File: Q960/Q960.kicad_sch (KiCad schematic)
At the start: 9 parts, among them J101 BAT(3V), J102 BAT(3V), SW101 INCL, U101 SeeeduinoXIAO

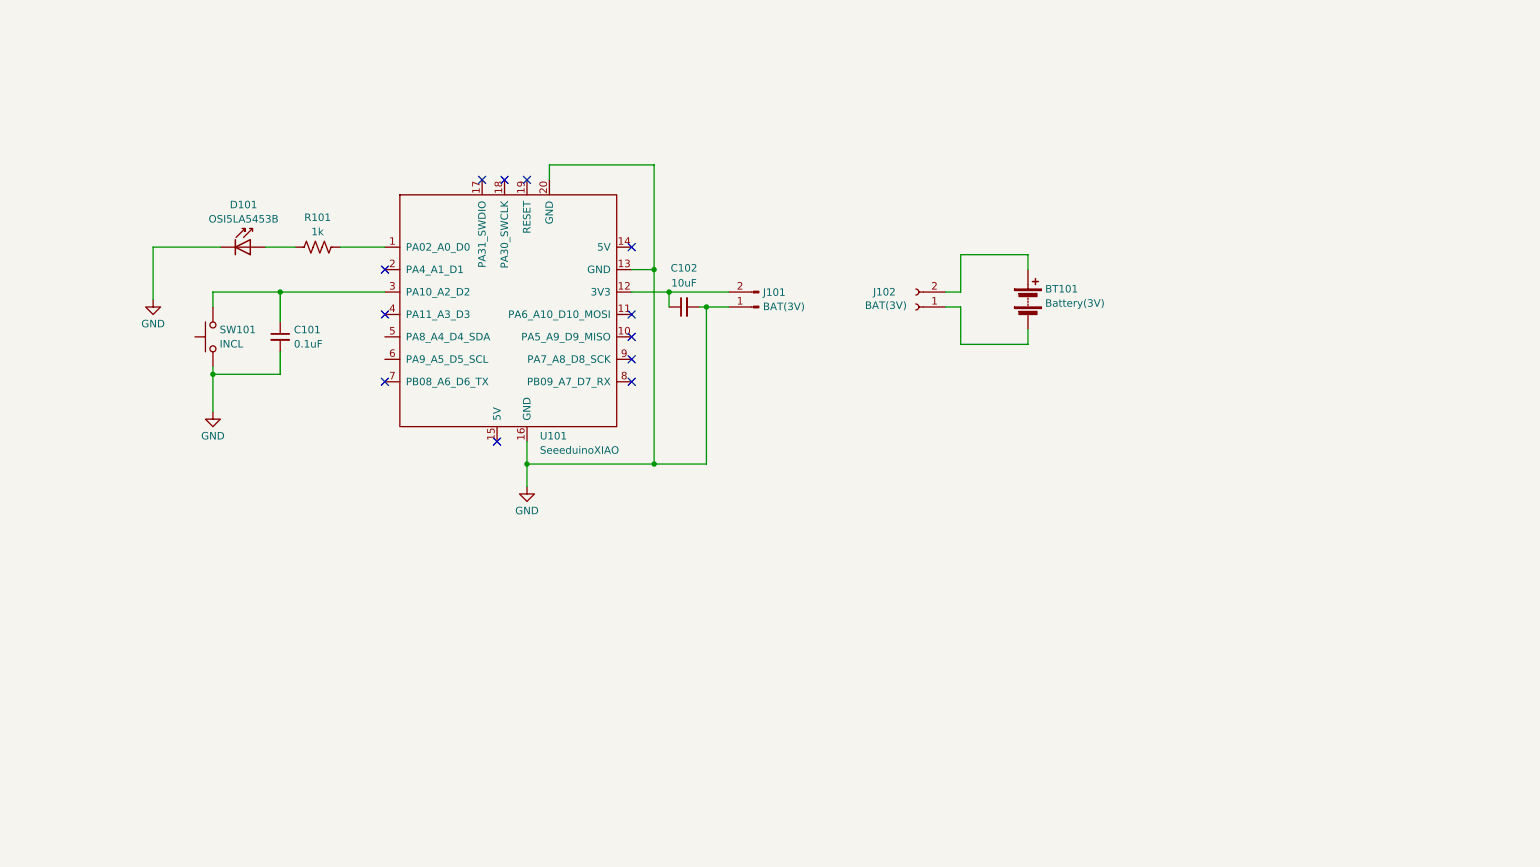
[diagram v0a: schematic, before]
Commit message: Rotary corded switch add
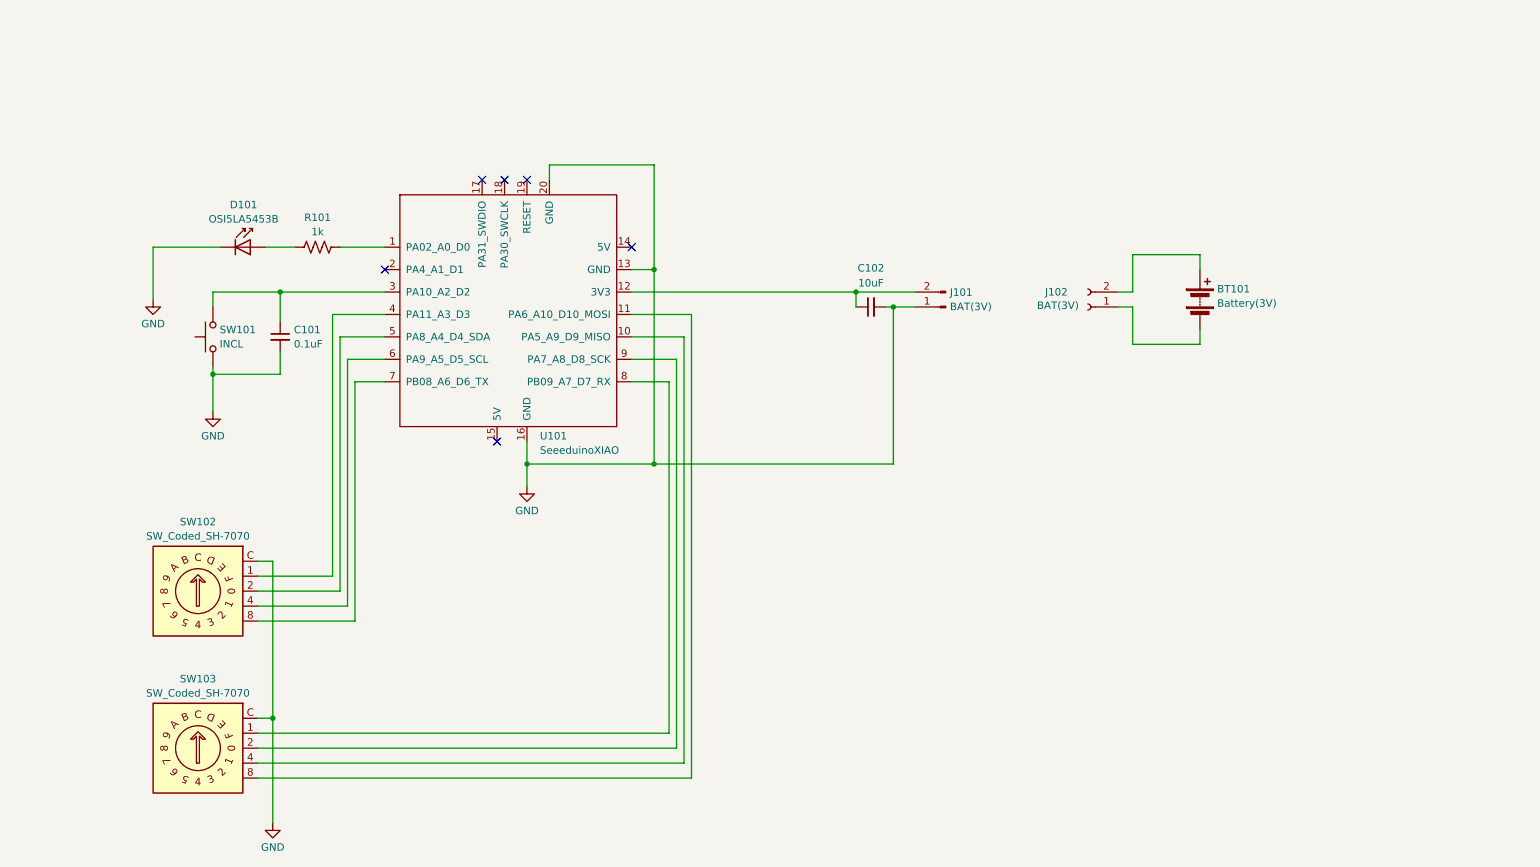
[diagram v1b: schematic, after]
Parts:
- added SW102, SW103: SW_Coded_SH-7070, Button_Switch_SMD:Nidec_Copal_SH-7010B, symbol Switch:SW_Coded_SH-7070
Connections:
- net GND: now also SW102.C, SW103.C
- net at U101.10 (PA5_A9_D9_MISO): now also SW103.4
- net at U101.11 (PA6_A10_D10_MOSI): now also SW103.8
- net at U101.4 (PA11_A3_D3): now also SW102.1
- net at U101.5 (PA8_A4_D4_SDA): now also SW102.2
- net at U101.6 (PA9_A5_D5_SCL): now also SW102.4
- net at U101.7 (PB08_A6_D6_TX): now also SW102.8
- net at U101.8 (PB09_A7_D7_RX): now also SW103.1
- net at U101.9 (PA7_A8_D8_SCK): now also SW103.2
- no-connect marks 12 -> 6
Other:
- moved on the sheet: BT101, C102, J101, J102

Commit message: エンコーダフットマーク考え中
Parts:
- R101: value 1k -> 100
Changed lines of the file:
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@@
 			)
 		)
-		(property "Datasheet" "https://www.nidec-copal-electronics.com/e/catalog/switch/sh-7000.pdf"
+		(property "Datasheet" "https://ja.aliexpress.com/item/4000917906566.html?gatewayAdapt=glo2jpn"
 			(at 59.69 130.81 0)
 			(effects
@@
 			)
 		)
-		(property "Value" "1k"
+		(property "Value" "100"
 			(at 80.01 69.7808 90)
 			(effects
@@
 			)
 		)
-		(property "Datasheet" "https://www.nidec-copal-electronics.com/e/catalog/switch/sh-7000.pdf"
+		(property "Datasheet" "https://ja.aliexpress.com/item/4000917906566.html?gatewayAdapt=glo2jpn"
 			(at 59.69 157.48 0)
 			(effects

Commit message: ロータリエンコーダを選択中
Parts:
- removed SW102, SW103: SW_Coded_SH-7070, Button_Switch_SMD:Nidec_Copal_SH-7010B, symbol Switch:SW_Coded_SH-7070
- added U102, U103: ~, HOLLY2:SW_CODED_4bit_SMD, symbol holly:SW_CODED_0-F
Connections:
- net GND: now also U102.C, U103.C; no longer U101.16 (GND), U101.20 (GND)
- net at U101.4 (PA11_A3_D3): now also U102.1
- net at U101.5 (PA8_A4_D4_SDA): now also U102.2
- net at U101.6 (PA9_A5_D5_SCL): now also U102.4
- net at U101.7 (PB08_A6_D6_TX): now also U102.8
- net at U101.8 (PB09_A7_D7_RX): now also U103.1
- net at U101.9 (PA7_A8_D8_SCK): now also U103.2
- net at U101.10 (PA5_A9_D9_MISO): now also U103.4
- net at U101.11 (PA6_A10_D10_MOSI): now also U103.8
- no-connect marks 6 -> 8
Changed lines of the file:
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@@
-	)
-	(junction
-		(at 137.16 76.2)
-		(diameter 0)
-		(color 0 0 0 0)
-	)
-	(junction
-		(at 115.57 109.22)
-		(diameter 0)
-		(color 0 0 0 0)
 	)
 	(junction
@@
 	)
 	(no_connect
+		(at 119.38 60.96)
+	)
+	(no_connect
 		(at 107.95 60.96)
+	)
+	(no_connect
+		(at 115.57 105.41)
 	)
 	(no_connect
@@
 	(wire
 		(pts
-			(xy 115.57 109.22) (xy 115.57 113.03)
+			(xy 133.35 109.22) (xy 133.35 113.03)
 		)
 		(stroke
@@
 	(wire
 		(pts
-			(xy 137.16 58.42) (xy 137.16 76.2)
-		)
-		(stroke
-			(width 0)
-			(type default)
-		)
-	)
-	(wire
-		(pts
 			(xy 139.7 154.94) (xy 69.85 154.94)
 		)
@@
 	(wire
 		(pts
-			(xy 137.16 109.22) (xy 115.57 109.22)
+			(xy 137.16 109.22) (xy 133.35 109.22)
 		)
 		(stroke
@@
 	(wire
 		(pts
-			(xy 119.38 58.42) (xy 137.16 58.42)
-		)
-		(stroke
-			(width 0)
-			(type default)
-		)
-	)
-	(wire
-		(pts
 			(xy 218.44 82.55) (xy 218.44 88.9)
 		)
@@
 	(wire
 		(pts
-			(xy 115.57 105.41) (xy 115.57 109.22)
-		)
-		(stroke
-			(width 0)
-			(type default)
-		)
-	)
-	(wire
-		(pts
 			(xy 69.85 125.73) (xy 72.39 125.73)
 		)
@@
 		(pts
 			(xy 71.12 72.39) (xy 76.2 72.39)
-		)
-		(stroke
-			(width 0)
-			(type default)
-		)
-	)
-	(wire
-		(pts
-			(xy 119.38 60.96) (xy 119.38 58.42)
 		)
 		(stroke
@@
 	)
 	(symbol
+		(lib_id "holly:SW_CODED_0-F")
+		(at 60.96 123.19 0)
+		(unit 1)
+		(exclude_from_sim no)
+		(in_bom yes)
+		(on_board yes)
+		(dnp no)
+		(fields_autoplaced yes)
+		(property "Reference" "U102"
+			(at 61.468 121.9285 0)
+			(effects
+				(font
+					(size 1.27 1.27)
+				)
+			)
+		)
+		(property "Value" "~"
+			(at 61.468 123.6099 0)
+			(effects
+				(font
+					(size 1.27 1.27)
+				)
+			)
+		)
+		(property "Footprint" "HOLLY2:SW_CODED_4bit_SMD"
+			(at 60.96 123.19 0)
+			(effects
+				(font
+					(size 1.27 1.27)
+				)
+				(hide yes)
+			)
+		)
+		(property "Datasheet" ""
+			(at 60.96 123.19 0)
+			(effects
+				(font
+					(size 1.27 1.27)
+				)
+				(hide yes)
+			)
+		)
+		(property "Description" ""
+			(at 60.96 123.19 0)
+			(effects
+				(font
+					(size 1.27 1.27)
+				)
+				(hide yes)
+			)
+		)
+		(pin "2"
+		)
+		(pin "8"
+		)
+		(pin "C"
+		)
+		(pin "4"
+		)
+		(pin "1"
+		)
+		(instances
+			(project ""
+				(path "/aa9b1917-073a-48a7-b08f-90b406395592"
+					(reference "U102")
+					(unit 1)
+				)
+			)
+		)
+	)
+	(symbol
 		(lib_id "Device:Battery")
 		(at 229.87 81.28 0)
@@
 				(path "/aa9b1917-073a-48a7-b08f-90b406395592"
 					(reference "BT101")
+					(unit 1)
+				)
+			)
+		)
+	)
+	(symbol
+		(lib_id "holly:SW_CODED_0-F")
+		(at 60.96 149.86 0)
+		(unit 1)
+		(exclude_from_sim no)
+		(in_bom yes)
+		(on_board yes)
+		(dnp no)
+		(fields_autoplaced yes)
+		(property "Reference" "U103"
+			(at 61.468 148.5985 0)
+			(effects
+				(font
+					(size 1.27 1.27)
+				)
+			)
+		)
+		(property "Value" "~"
+			(at 61.468 150.2799 0)
+			(effects
+				(font
+					(size 1.27 1.27)
+				)
+			)
+		)
+		(property "Footprint" "HOLLY2:SW_CODED_4bit_SMD"
+			(at 60.96 149.86 0)
+			(effects
+				(font
+					(size 1.27 1.27)
+				)
+				(hide yes)
+			)
+		)
+		(property "Datasheet" ""
+			(at 60.96 149.86 0)
+			(effects
+				(font
+					(size 1.27 1.27)
+				)
+				(hide yes)
+			)
+		)
+		(property "Description" ""
+			(at 60.96 149.86 0)
+			(effects
+				(font
+					(size 1.27 1.27)
+				)
+				(hide yes)
+			)
+		)
+		(pin "2"
+		)
+		(pin "8"
+		)
+		(pin "C"
+		)
+		(pin "4"
+		)
+		(pin "1"
+		)
+		(instances
+			(project ""
+				(path "/aa9b1917-073a-48a7-b08f-90b406395592"
+					(reference "U103")
 					(unit 1)
 				)
@@
 	)
 	(symbol
-		(lib_id "Switch:SW_Coded_SH-7070")
-		(at 59.69 130.81 0)
-		(unit 1)
-		(exclude_from_sim no)
-		(in_bom yes)
-		(on_board yes)
-		(dnp no)
-		(fields_autoplaced yes)
-		(property "Reference" "SW102"
-			(at 59.69 119.0455 0)
-			(effects
-				(font
-					(size 1.27 1.27)
-				)
-			)
-		)
-		(property "Value" "SW_Coded_SH-7070"
-			(at 59.69 121.4698 0)
-			(effects
-				(font
-					(size 1.27 1.27)
-				)
-			)
-		)
-		(property "Footprint" "Button_Switch_SMD:Nidec_Copal_SH-7010B"
-			(at 52.07 142.24 0)
-			(effects
-				(font
-					(size 1.27 1.27)
-				)
-				(justify left)
-				(hide yes)
-			)
-		)
-		(property "Datasheet" "https://ja.aliexpress.com/item/4000917906566.html?gatewayAdapt=glo2jpn"
-			(at 59.69 130.81 0)
-			(effects
-				(font
-					(size 1.27 1.27)
-				)
-				(hide yes)
-			)
-		)
-		(property "Description" "Rotary switch, 4-bit encoding, 16 positions, Complementary code"
-			(at 59.69 130.81 0)
-			(effects
-				(font
-					(size 1.27 1.27)
-				)
-				(hide yes)
-			)
-		)
-		(pin "4"
-		)
-		(pin "2"
-		)
-		(pin "8"
-		)
-		(pin "1"
-		)
-		(pin "C"
-		)
-		(instances
-			(project ""
-				(path "/aa9b1917-073a-48a7-b08f-90b406395592"
-					(reference "SW102")
-					(unit 1)
-				)
-			)
-		)
-	)
-	(symbol
 		(lib_id "Device:R_US")
 		(at 80.01 72.39 90)
@@
 	(symbol
 		(lib_id "power:GND")
-		(at 115.57 113.03 0)
+		(at 133.35 113.03 0)
 		(unit 1)
 		(exclude_from_sim no)
@@
 		(fields_autoplaced yes)
 		(property "Reference" "#PWR0102"
-			(at 115.57 119.38 0)
+			(at 133.35 119.38 0)
 			(effects
 				(font
@@
 		)
 		(property "Value" "GND"
-			(at 115.57 117.1631 0)
+			(at 133.35 117.1631 0)
 			(effects
 				(font
@@
 		)
 		(property "Footprint" ""
-			(at 115.57 113.03 0)
+			(at 133.35 113.03 0)
 			(effects
 				(font
@@
 		)
 		(property "Datasheet" ""
-			(at 115.57 113.03 0)
+			(at 133.35 113.03 0)
 			(effects
 				(font
@@
 		)
 		(property "Description" "Power symbol creates a global label with name \"GND\" , ground"
-			(at 115.57 113.03 0)
+			(at 133.35 113.03 0)
 			(effects
 				(font
@@
 					(unit 1)
 				)
-			)
-		)
-	)
-	(symbol
-		(lib_id "Switch:SW_Coded_SH-7070")
-		(at 59.69 157.48 0)
-		(unit 1)
-		(exclude_from_sim no)
-		(in_bom yes)
-		(on_board yes)
-		(dnp no)
-		(fields_autoplaced yes)
-		(property "Reference" "SW103"
-			(at 59.69 145.7155 0)
-			(effects
-				(font
-					(size 1.27 1.27)
-				)
-			)
-		)
-		(property "Value" "SW_Coded_SH-7070"
-			(at 59.69 148.1398 0)
-			(effects
-				(font
-					(size 1.27 1.27)
-				)
-			)
-		)
-		(property "Footprint" "Button_Switch_SMD:Nidec_Copal_SH-7010B"
-			(at 52.07 168.91 0)
-			(effects
-				(font
-					(size 1.27 1.27)
-				)
-				(justify left)
-				(hide yes)
-			)
-		)
-		(property "Datasheet" "https://ja.aliexpress.com/item/4000917906566.html?gatewayAdapt=glo2jpn"
-			(at 59.69 157.48 0)
-			(effects
-				(font
-					(size 1.27 1.27)
-				)
-				(hide yes)
-			)
-		)
-		(property "Description" "Rotary switch, 4-bit encoding, 16 positions, Complementary code"
-			(at 59.69 157.48 0)
-			(effects
-				(font
-					(size 1.27 1.27)
-				)
-				(hide yes)
-			)
-		)
-		(pin "1"
-		)
-		(pin "2"
-		)
-		(pin "4"
-		)
-		(pin "8"
-		)
-		(pin "C"
-		)
-		(instances
-			(project ""
-				(path "/aa9b1917-073a-48a7-b08f-90b406395592"
-					(reference "SW103")
-					(unit 1)
-				)

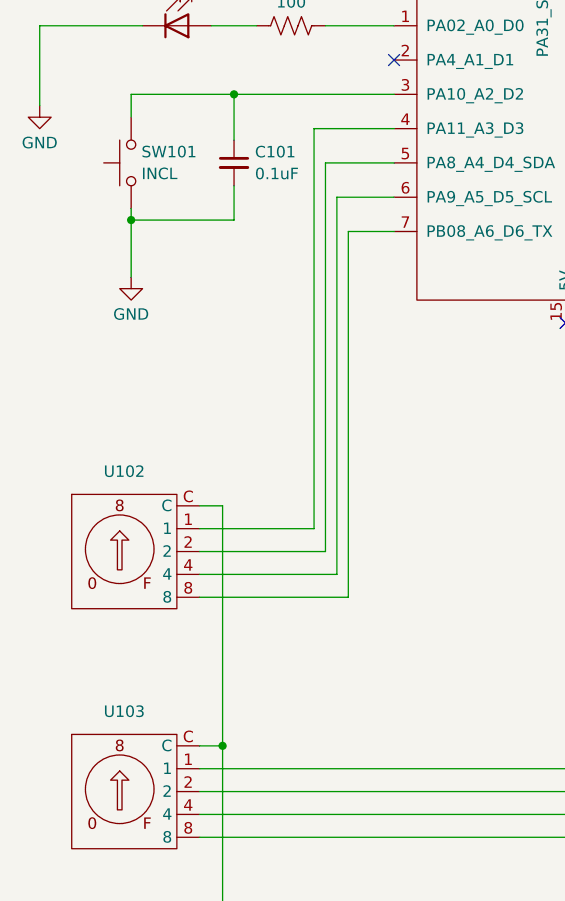
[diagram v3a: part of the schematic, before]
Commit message: U102,103を挿入部品に変更
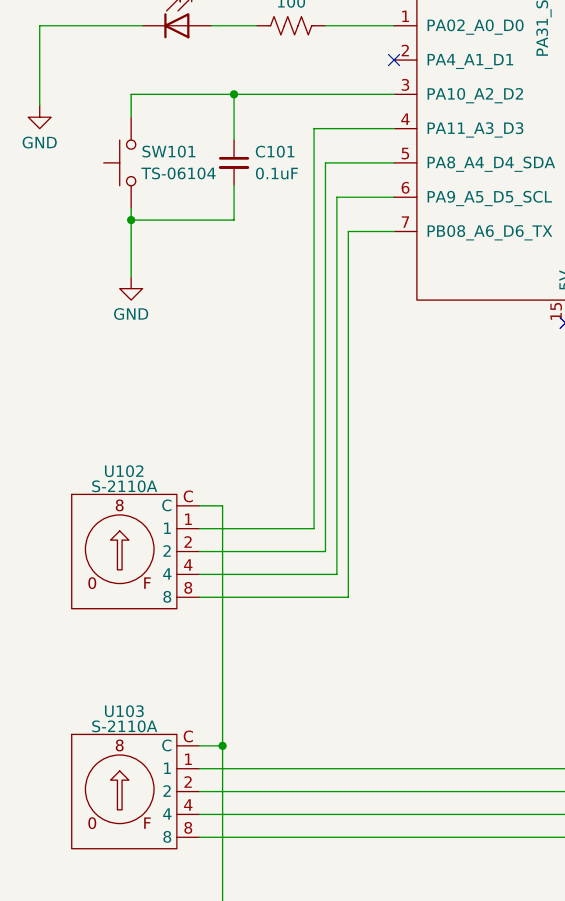
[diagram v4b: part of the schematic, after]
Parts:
- SW101: value INCL -> TS-06104
- U102, U103: value ~ -> S-2110A; footprint HOLLY2:SW_CODED_4bit_SMD -> HOLLY2:S-2110A
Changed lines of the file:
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@@
 		(exclude_from_sim no)
 		(in_bom yes)
-		(on_board no)
+		(on_board yes)
 		(dnp no)
 		(fields_autoplaced yes)
@@
 			)
 		)
-		(property "Value" "INCL"
+		(property "Value" "TS-06104"
 			(at 63.373 88.8421 90)
 			(effects
@@
 			)
 		)
-		(property "Datasheet" "~"
+		(property "Datasheet" "https://akizukidenshi.com/goodsaffix/TS-06104.pdf"
 			(at 57.15 87.63 0)
 			(effects
@@
 			)
 		)
-		(property "Value" "~"
+		(property "Value" "S-2110A"
 			(at 61.468 123.6099 0)
 			(effects
@@
 			)
 		)
-		(property "Footprint" "HOLLY2:SW_CODED_4bit_SMD"
+		(property "Footprint" "HOLLY2:S-2110A"
 			(at 60.96 123.19 0)
 			(effects
@@
 			)
 		)
-		(property "Datasheet" ""
+		(property "Datasheet" "https://akizukidenshi.com/goodsaffix/s1000a_2000a.pdf"
 			(at 60.96 123.19 0)
 			(effects
@@
 			)
 		)
-		(property "Description" ""
+		(property "Description" "ROTARY CODED SWITCH"
 			(at 60.96 123.19 0)
 			(effects
@@
 			)
 		)
-		(property "Value" "~"
+		(property "Value" "S-2110A"
 			(at 61.468 150.2799 0)
 			(effects
@@
 			)
 		)
-		(property "Footprint" "HOLLY2:SW_CODED_4bit_SMD"
+		(property "Footprint" "HOLLY2:S-2110A"
 			(at 60.96 149.86 0)
 			(effects
@@
 			)
 		)
-		(property "Datasheet" ""
+		(property "Datasheet" "https://akizukidenshi.com/goodsaffix/s1000a_2000a.pdf"
 			(at 60.96 149.86 0)
 			(effects

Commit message: Rotary encoded switch append
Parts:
- SW101: footprint (none) -> HOLLY2:TVDT18-050
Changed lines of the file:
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@@
 			)
 		)
-		(property "Footprint" ""
+		(property "Footprint" "HOLLY2:TVDT18-050"
 			(at 57.15 87.63 0)
 			(effects

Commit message: Ver:1.00 Released
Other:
- company: (none) -> AMPSD
- title: (none) -> IrBeacon Transmitter
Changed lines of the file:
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@@
 	(generator_version "8.0")
 	(paper "A4")
+	(title_block
+		(title "IrBeacon Transmitter")
+		(date "2024-07-31")
+		(rev "1.00")
+		(company "AMPSD")
+	)
 	(junction
 		(at 62.23 93.98)

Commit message: 途中
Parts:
- R101: value 100 -> 47
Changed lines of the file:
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@@
 	(title_block
 		(title "IrBeacon Transmitter")
-		(date "2024-07-31")
-		(rev "1.00")
+		(date "2024-11-14")
+		(rev "1.10")
 		(company "AMPSD")
+		(comment 1 "R101を100から47Ωに変更")
 	)
 	(junction
@@
 			)
 		)
-		(property "Value" "100"
+		(property "Value" "47"
 			(at 80.01 69.7808 90)
 			(effects
